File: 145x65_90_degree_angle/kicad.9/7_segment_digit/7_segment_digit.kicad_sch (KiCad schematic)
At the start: 10 parts, among them X1 PLS-10

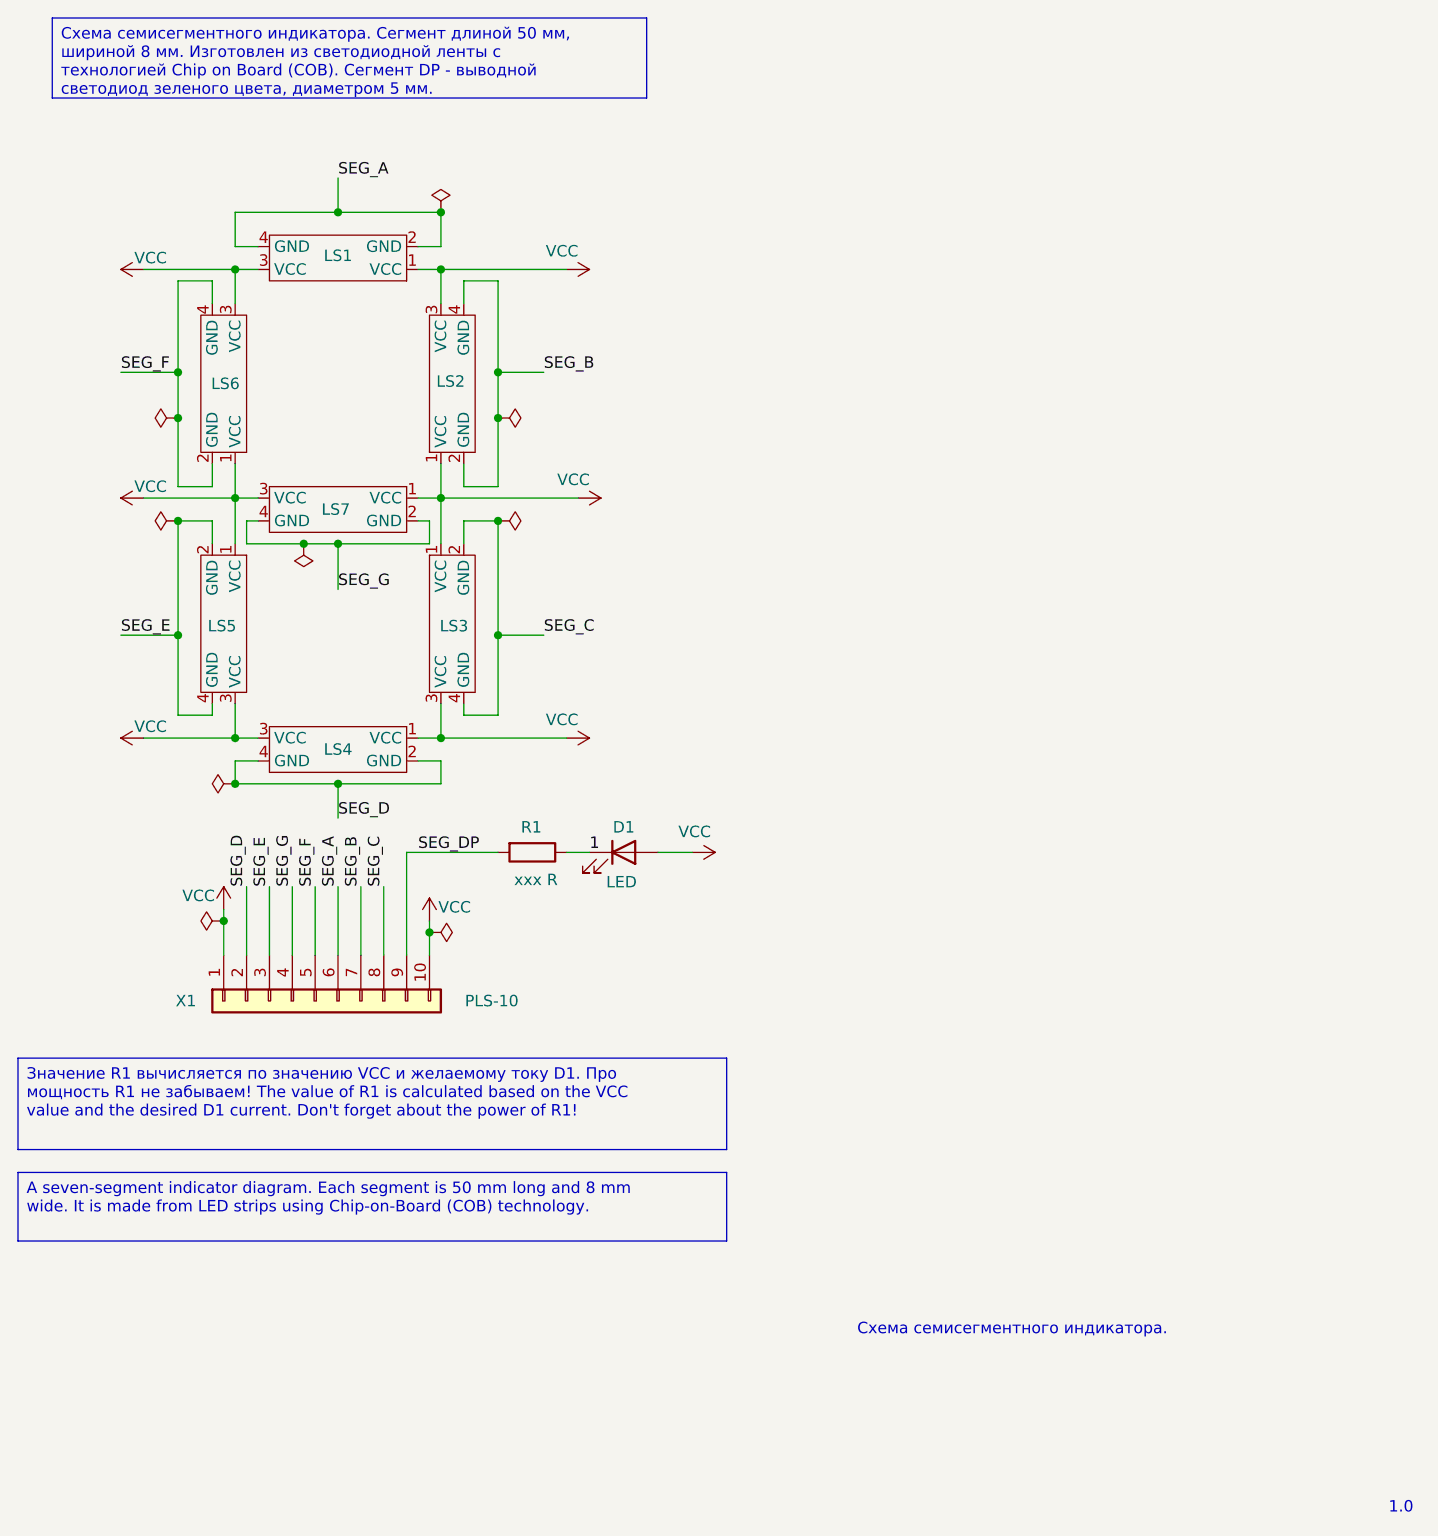
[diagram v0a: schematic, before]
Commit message: Добавил символ и посадочную площадку СИД SMD 5050. Обновил схему и ПП.
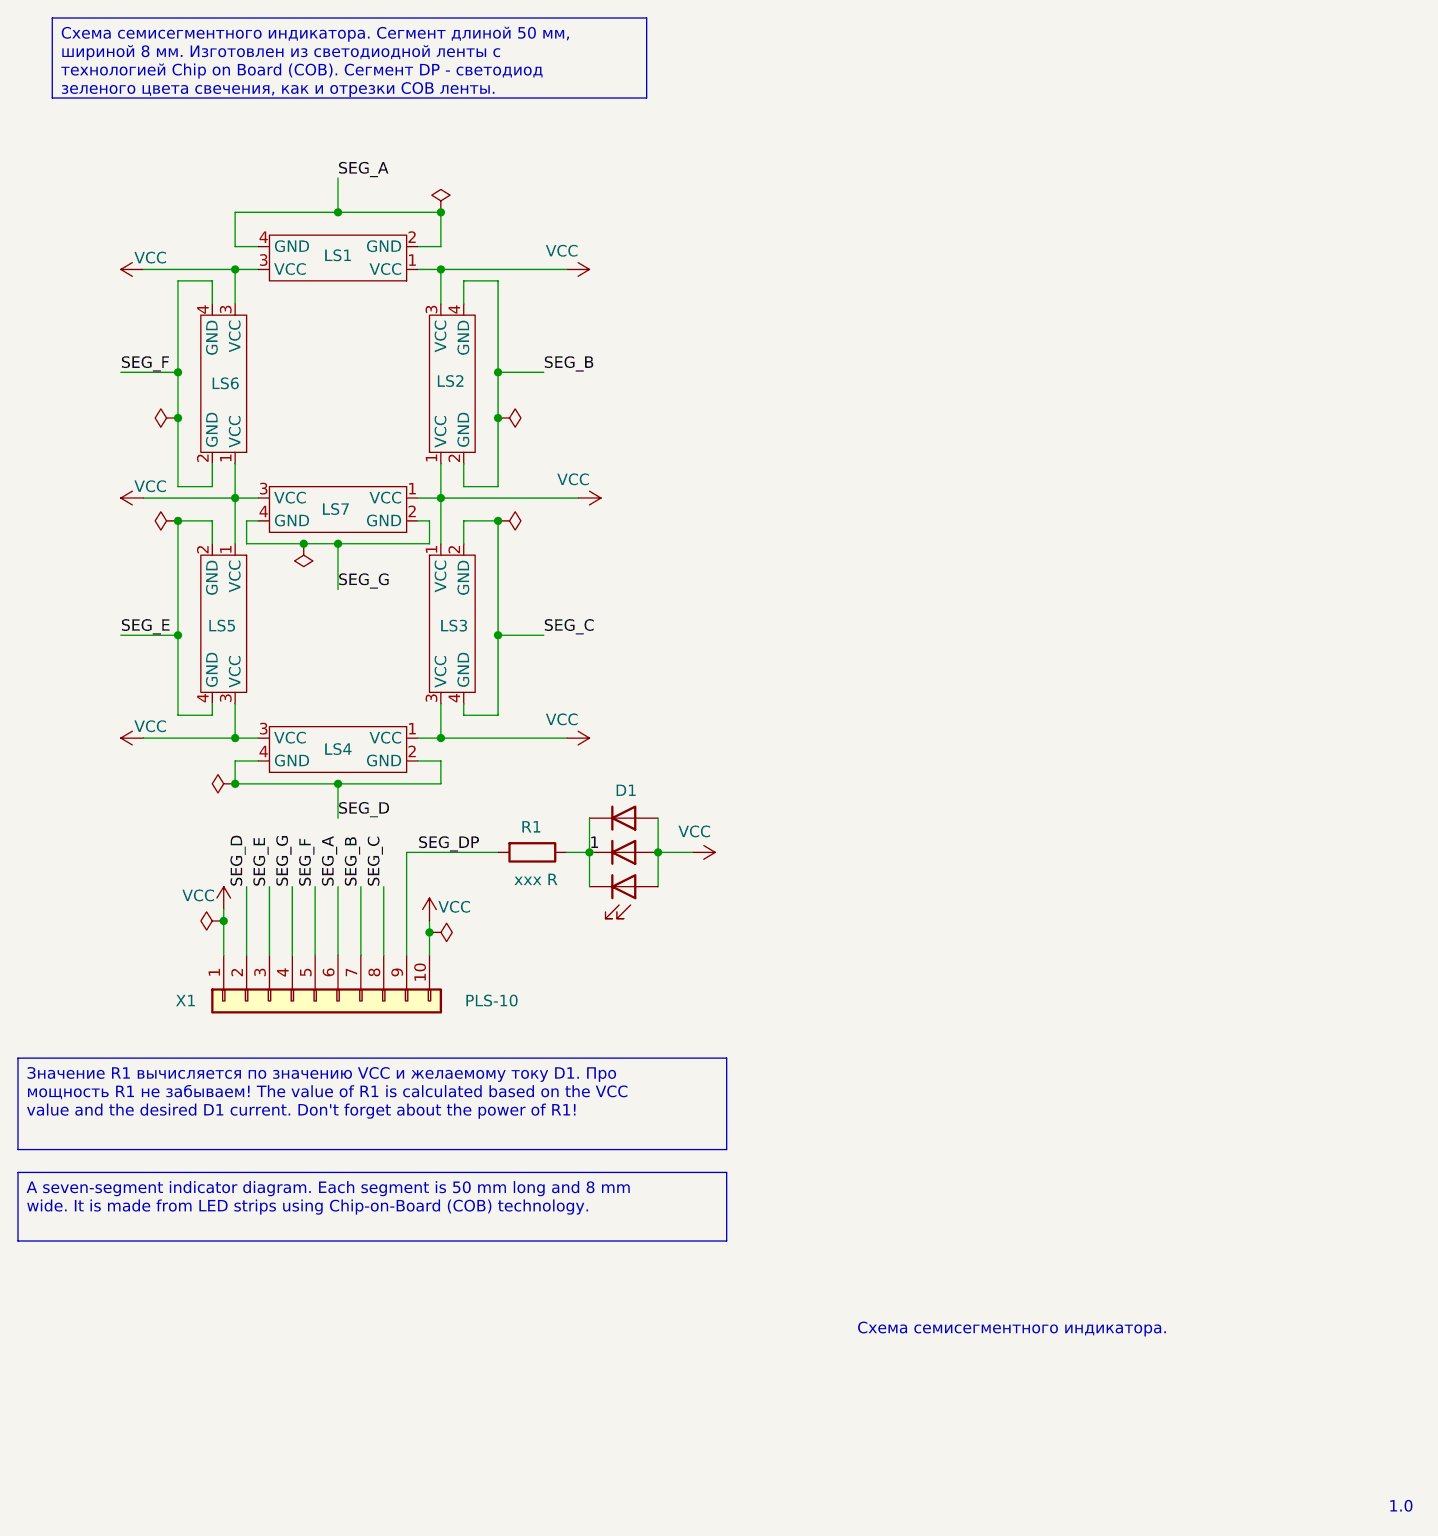
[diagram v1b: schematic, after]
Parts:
- removed D1: LED, LED_THT:LED_D5.0mm, symbol Device:LED
- added D1: ~, led_strip:LED_SMD_5050_6, symbol 7_segment_digit:Diode
- LS1: footprint led_strip:led_strip_50mm_len_8mm_height_TH -> led_strip:led_strip_50mm_len_8mm_height
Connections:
- net 1: now also D1.2 (K0), D1.4 (K1), D1.6 (K2)
- net VCC: now also D1.1 (A0), D1.3 (A1), D1.5 (A2)
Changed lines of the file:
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@@
 		)
 	)
-	(text_box "Схема семисегментного индикатора. Сегмент длиной 50 мм, шириной 8 мм. Изготовлен из светодиодной ленты с технологией Chip on Board (COB). Сегмент DP - выводной светодиод зеленого цвета, диаметром 5 мм."
+	(text_box "Схема семисегментного индикатора. Сегмент длиной 50 мм, шириной 8 мм. Изготовлен из светодиодной ленты с технологией Chip on Board (COB). Сегмент DP - светодиод зеленого цвета свечения, как и отрезки COB ленты."
 		(exclude_from_sim no)
 		(at 120.65 27.94 0)
@@
 	)
 	(junction
+		(at 180.34 120.65)
+		(diameter 0)
+		(color 0 0 0 0)
+	)
+	(junction
 		(at 170.18 83.82)
 		(diameter 0)
@@
 	)
 	(junction
+		(at 187.96 120.65)
+		(diameter 0)
+		(color 0 0 0 0)
+	)
+	(junction
 		(at 170.18 72.39)
 		(diameter 0)
@@
 	(wire
 		(pts
+			(xy 187.96 120.65) (xy 187.96 124.46)
+		)
+		(stroke
+			(width 0)
+			(type default)
+		)
+	)
+	(wire
+		(pts
 			(xy 140.97 81.28) (xy 140.97 86.36)
 		)
@@
 	(wire
 		(pts
+			(xy 187.96 116.84) (xy 187.96 120.65)
+		)
+		(stroke
+			(width 0)
+			(type default)
+		)
+	)
+	(wire
+		(pts
 			(xy 160.02 120.65) (xy 160.02 132.08)
 		)
@@
 		(pts
 			(xy 166.37 57.15) (xy 166.37 59.69)
+		)
+		(stroke
+			(width 0)
+			(type default)
+		)
+	)
+	(wire
+		(pts
+			(xy 180.34 116.84) (xy 180.34 120.65)
+		)
+		(stroke
+			(width 0)
+			(type default)
+		)
+	)
+	(wire
+		(pts
+			(xy 180.34 120.65) (xy 180.34 124.46)
 		)
 		(stroke
@@
 	)
 	(symbol
+		(lib_id "7_segment_digit:Diode")
+		(at 180.34 120.65 0)
+		(unit 1)
+		(exclude_from_sim no)
+		(in_bom yes)
+		(on_board yes)
+		(dnp no)
+		(property "Reference" "D1"
+			(at 184.404 113.792 0)
+			(effects
+				(font
+					(size 1.27 1.27)
+				)
+			)
+		)
+		(property "Value" "~"
+			(at 183.8325 114.3 0)
+			(effects
+				(font
+					(size 1.27 1.27)
+				)
+			)
+		)
+		(property "Footprint" "led_strip:LED_SMD_5050_6"
+			(at 180.34 120.65 0)
+			(effects
+				(font
+					(size 1.27 1.27)
+				)
+				(hide yes)
+			)
+		)
+		(property "Datasheet" ""
+			(at 180.34 120.65 0)
+			(effects
+				(font
+					(size 1.27 1.27)
+				)
+				(hide yes)
+			)
+		)
+		(property "Description" ""
+			(at 180.34 120.65 0)
+			(effects
+				(font
+					(size 1.27 1.27)
+				)
+				(hide yes)
+			)
+		)
+		(pin "5"
+		)
+		(pin "1"
+		)
+		(pin "2"
+		)
+		(pin "6"
+		)
+		(pin "4"
+		)
+		(pin "3"
+		)
+		(instances
+			(project ""
+				(path "/5df25448-ca4f-4e12-a809-76052196b894"
+					(reference "D1")
+					(unit 1)
+				)
+			)
+		)
+	)
+	(symbol
 		(lib_id "7_segment_digit:led_strip_50mm_len_8mm_height")
 		(at 152.4 54.61 180)
@@
 			)
 		)
-		(property "Footprint" "led_strip:led_strip_50mm_len_8mm_height_TH"
+		(property "Footprint" "led_strip:led_strip_50mm_len_8mm_height"
 			(at 152.4 54.61 0)
 			(effects
@@
 					(unit 1)
 				)
-			)
-		)
-	)
-	(symbol
-		(lib_id "Device:LED")
-		(at 184.15 120.65 0)
-		(unit 1)
-		(exclude_from_sim no)
-		(in_bom yes)
-		(on_board yes)
-		(dnp no)
-		(property "Reference" "D1"
-			(at 184.15 117.856 0)
-			(effects
-				(font
-					(size 1.27 1.27)
-				)
-			)
-		)
-		(property "Value" "LED"
-			(at 183.896 123.952 0)
-			(effects
-				(font
-					(size 1.27 1.27)
-				)
-			)
-		)
-		(property "Footprint" "LED_THT:LED_D5.0mm"
-			(at 184.15 120.65 0)
-			(effects
-				(font
-					(size 1.27 1.27)
-				)
-				(hide yes)
-			)
-		)
-		(property "Datasheet" "~"
-			(at 184.15 120.65 0)
-			(effects
-				(font
-					(size 1.27 1.27)
-				)
-				(hide yes)
-			)
-		)
-		(property "Description" "Light emitting diode"
-			(at 184.15 120.65 0)
-			(effects
-				(font
-					(size 1.27 1.27)
-				)
-				(hide yes)
-			)
-		)
-		(property "Sim.Pins" "1=K 2=A"
-			(at 184.15 120.65 0)
-			(effects
-				(font
-					(size 1.27 1.27)
-				)
-				(hide yes)
-			)
-		)
-		(pin "1"
-		)
-		(pin "2"
-		)
-		(instances
-			(project ""
-				(path "/5df25448-ca4f-4e12-a809-76052196b894"
-					(reference "D1")
-					(unit 1)
-				)
